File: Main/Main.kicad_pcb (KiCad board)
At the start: 4 copper layers, 76.2 x 67.6 mm, 76 parts, among them J3 Conn_01x03, J4 Conn_01x03, J5 Conn_01x03, J6 Conn_01x03, SW1 SW_Push, SW2 SW_Push, U1 RP2350A-QFN60, U10 LM75B, U11 MCS1802GS-50-Z, U12 MCS1802GS-50-Z, U13 MCS1802GS-50-Z, U14 LM2575-3.3BT, U2 W25Q128JVS, U3 AMS1117-3.3, U4 MMC5983MA, U5 ICM-42688-P, U6 INA226, U7 KX134-1211, U8 MS5611-01BA, U9 MCS1802GS-50-Z, Y1 ABM8-272-T3

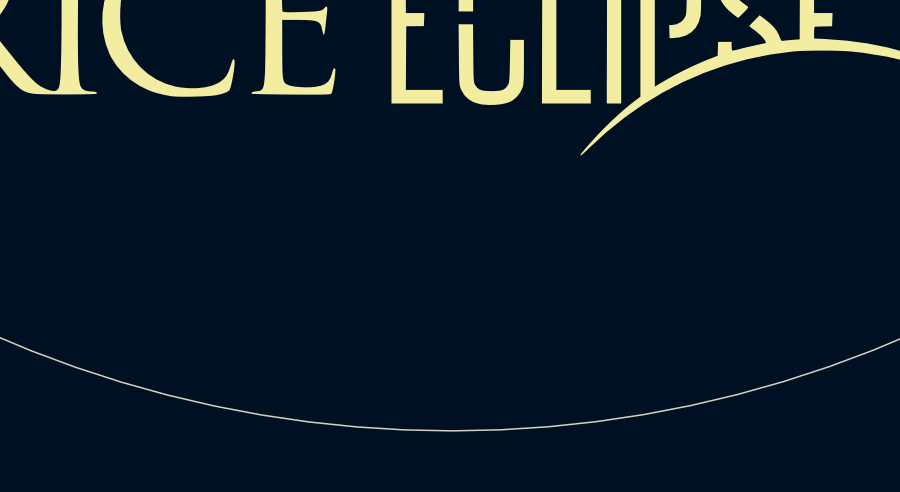
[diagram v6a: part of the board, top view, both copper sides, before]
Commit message: updated usb footprint
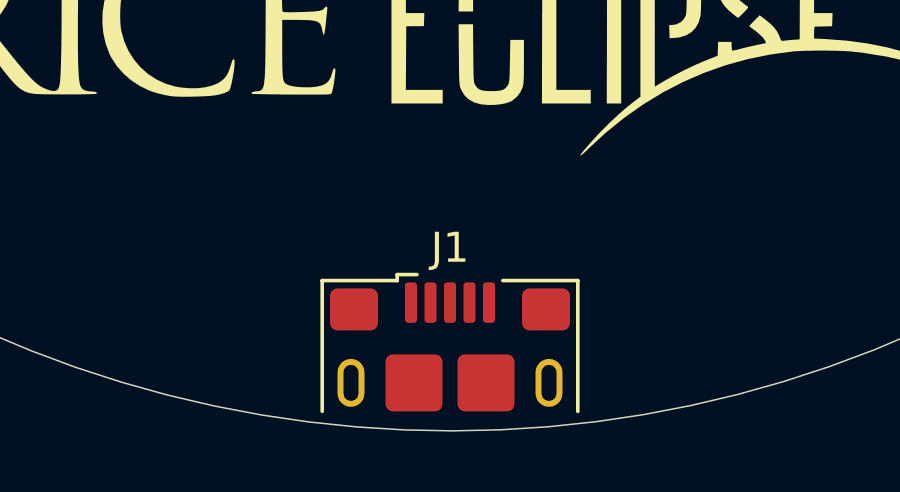
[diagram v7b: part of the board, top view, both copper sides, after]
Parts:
- added J1: USB_B_Micro, Connector_USB:USB_Micro-B_Amphenol_10118193-0001LF_Horizontal, F.Cu at (100.0, 136.5)

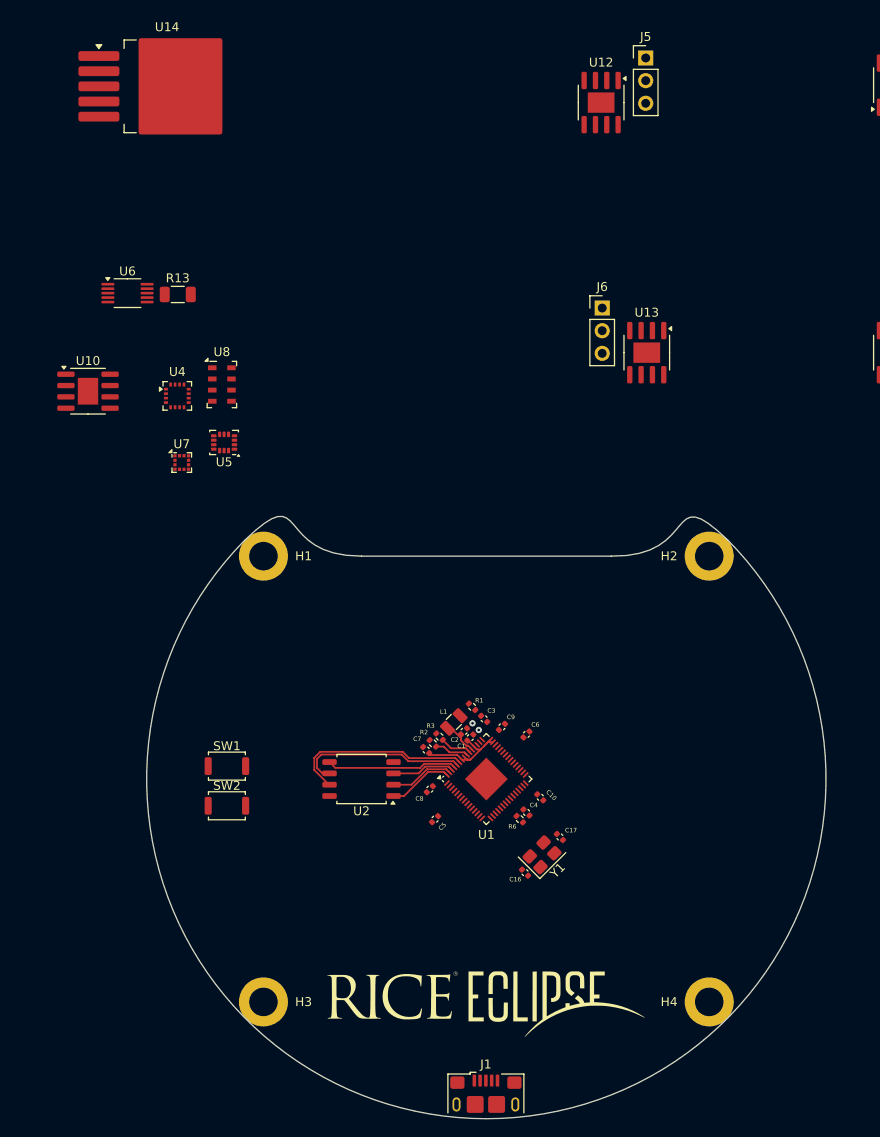
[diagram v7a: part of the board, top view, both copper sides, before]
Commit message: SD and USB footprint and model updated
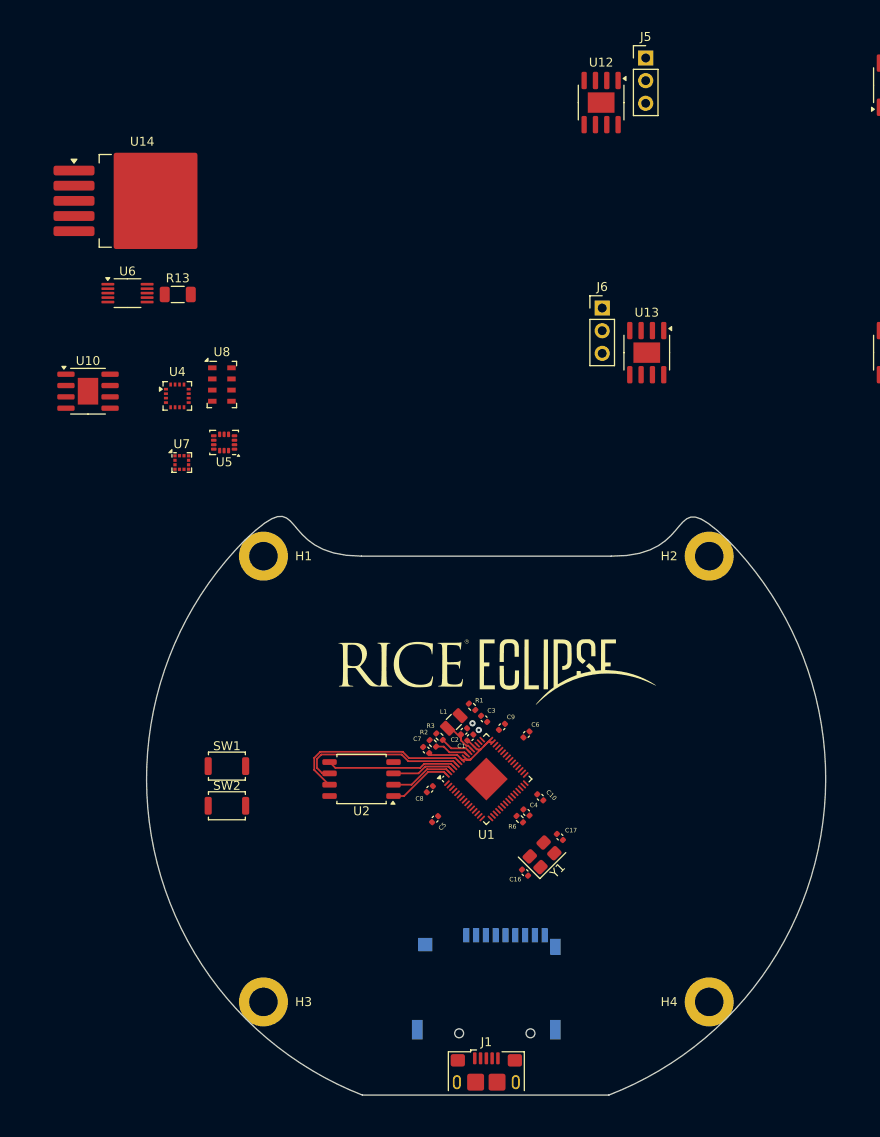
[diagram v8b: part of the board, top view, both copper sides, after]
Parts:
- added J7: MSD-4-A, otherComponents:CUI_MSD-4-A, B.Cu at (100.0, 125.3)
- moved G*** 37.3 mm to (101.2, 87.8)
- moved U14 13.1 mm to (61.4, 35.1)
- moved J1 2.50 mm to (100.0, 134.0)
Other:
- board size 76.2 x 67.6 mm -> 76.2 x 64.9 mm
